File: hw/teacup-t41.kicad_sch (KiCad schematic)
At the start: 104 parts, among them IC1 T31ZX, J1 USB Type-C, J10 AudioJack4_Ground, J11 Conn_01x04_Pin, J12 Conn_01x04_Pin, J13 SFW15R-2STE1LF, J14 Conn_01x02_MountingPin, J15 Conn_01x03_MountingPin, J16 Conn_01x03_MountingPin, J2 Micro_SD_Card, J3 USB_A, J4 Conn_02x08_Odd_Even, J5 UART, J6 Conn_02x07_Odd_Even, J7 Conn_02x07_Odd_Even, J8 DC_IN, J9 Conn_01x02_MountingPin, SW2 SW_SPDT, U1 AZ1117-3.3, U2 AZ1117-1.8, U3 MCP1826S, U4 W25Q32JVSS, U5 W25Q32JVSS, Y1 24 MHz

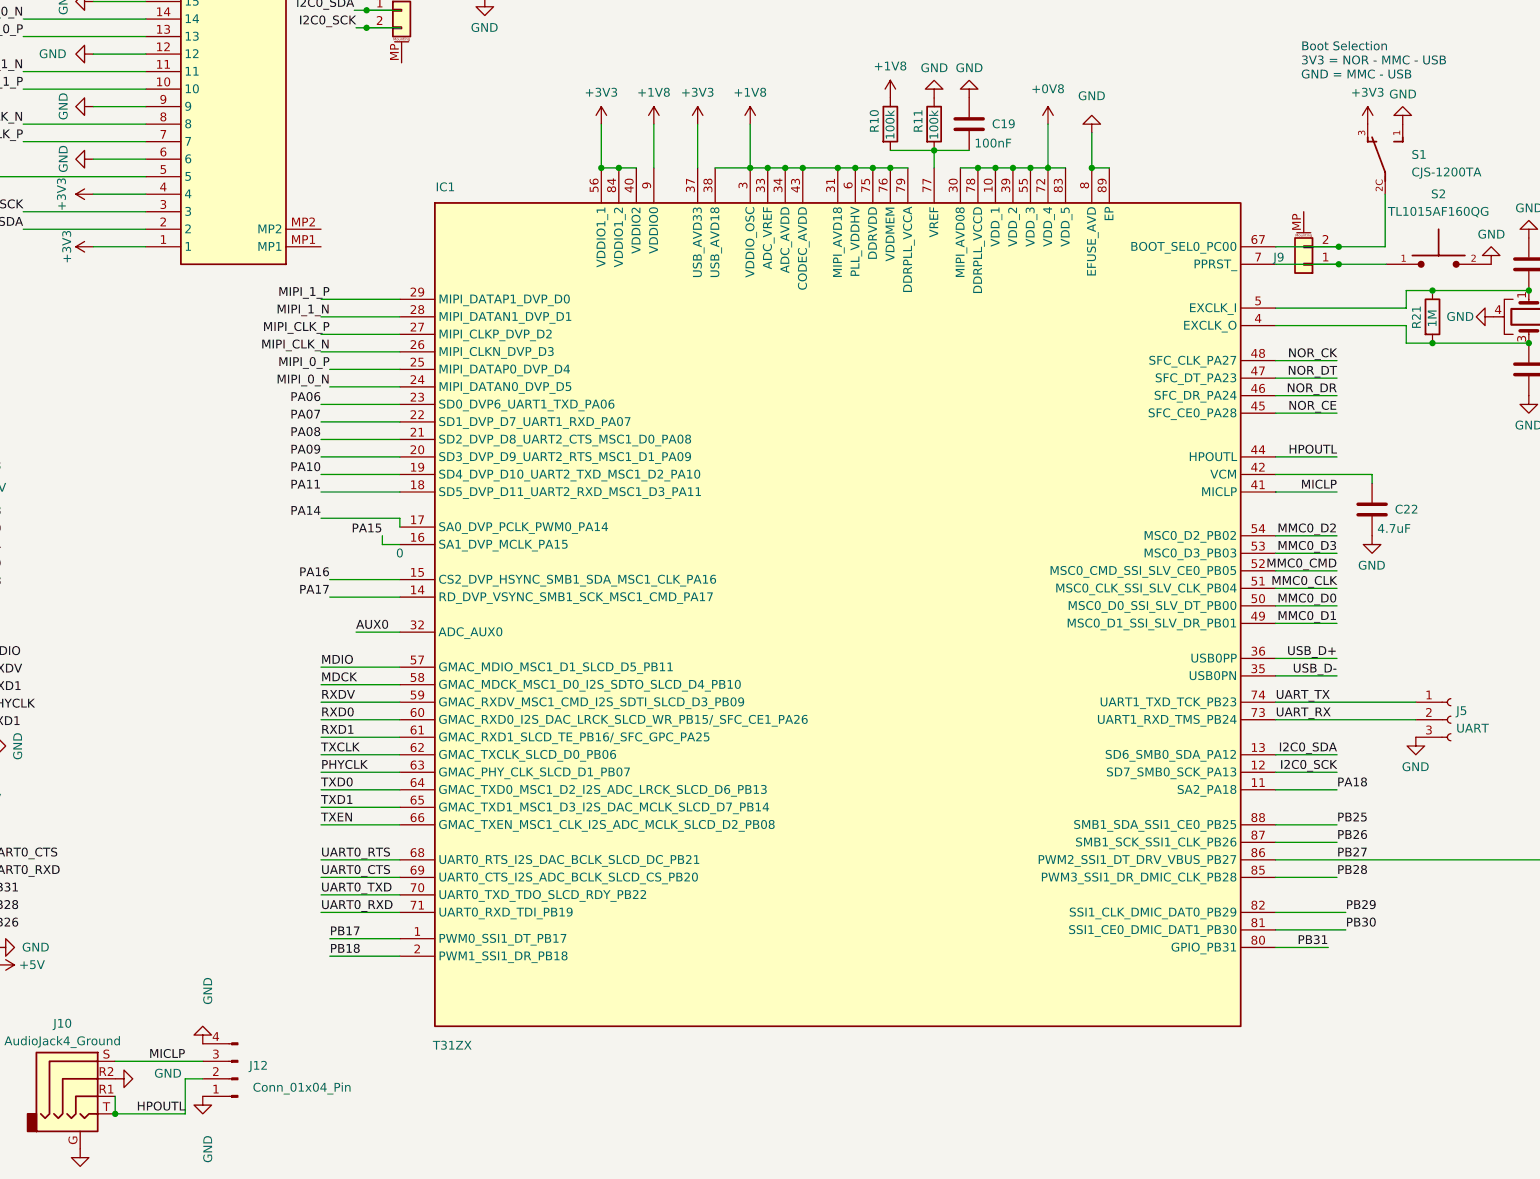
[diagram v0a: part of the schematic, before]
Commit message: Swap IC1 T31ZX->T41NQ in schematic, rewire by net-name
Label-driven rewire: T41NQ symbol placed, every pin connected per
t41_pin_nets.csv. 6 wire-only nets (crystal, boot-sel, VCM, DDR-VREF
divider, PB27/SD) re-anchored with reconnection labels; other stubs
removed with their inert far-labels. Auto-named nets given clean labels
(EXCLK_XIN/XOUT, BOOT_SEL0, VCM, DDR_VREF).

Verified via netlist export: all 97 IC1 pins on intended nets (0
mismatch), 0 peripheral nodes lost vs upstream (PPRST intentionally
dropped). Remaining ERC errors are pre-power-section: floating new
nets (DDR_ZQ/RZQ/POR_CTL/MICNL/NOR_WP/HOLD) + undriven +1V35 await
the power/new-circuit stage. gen_schematic.py in scripts/.
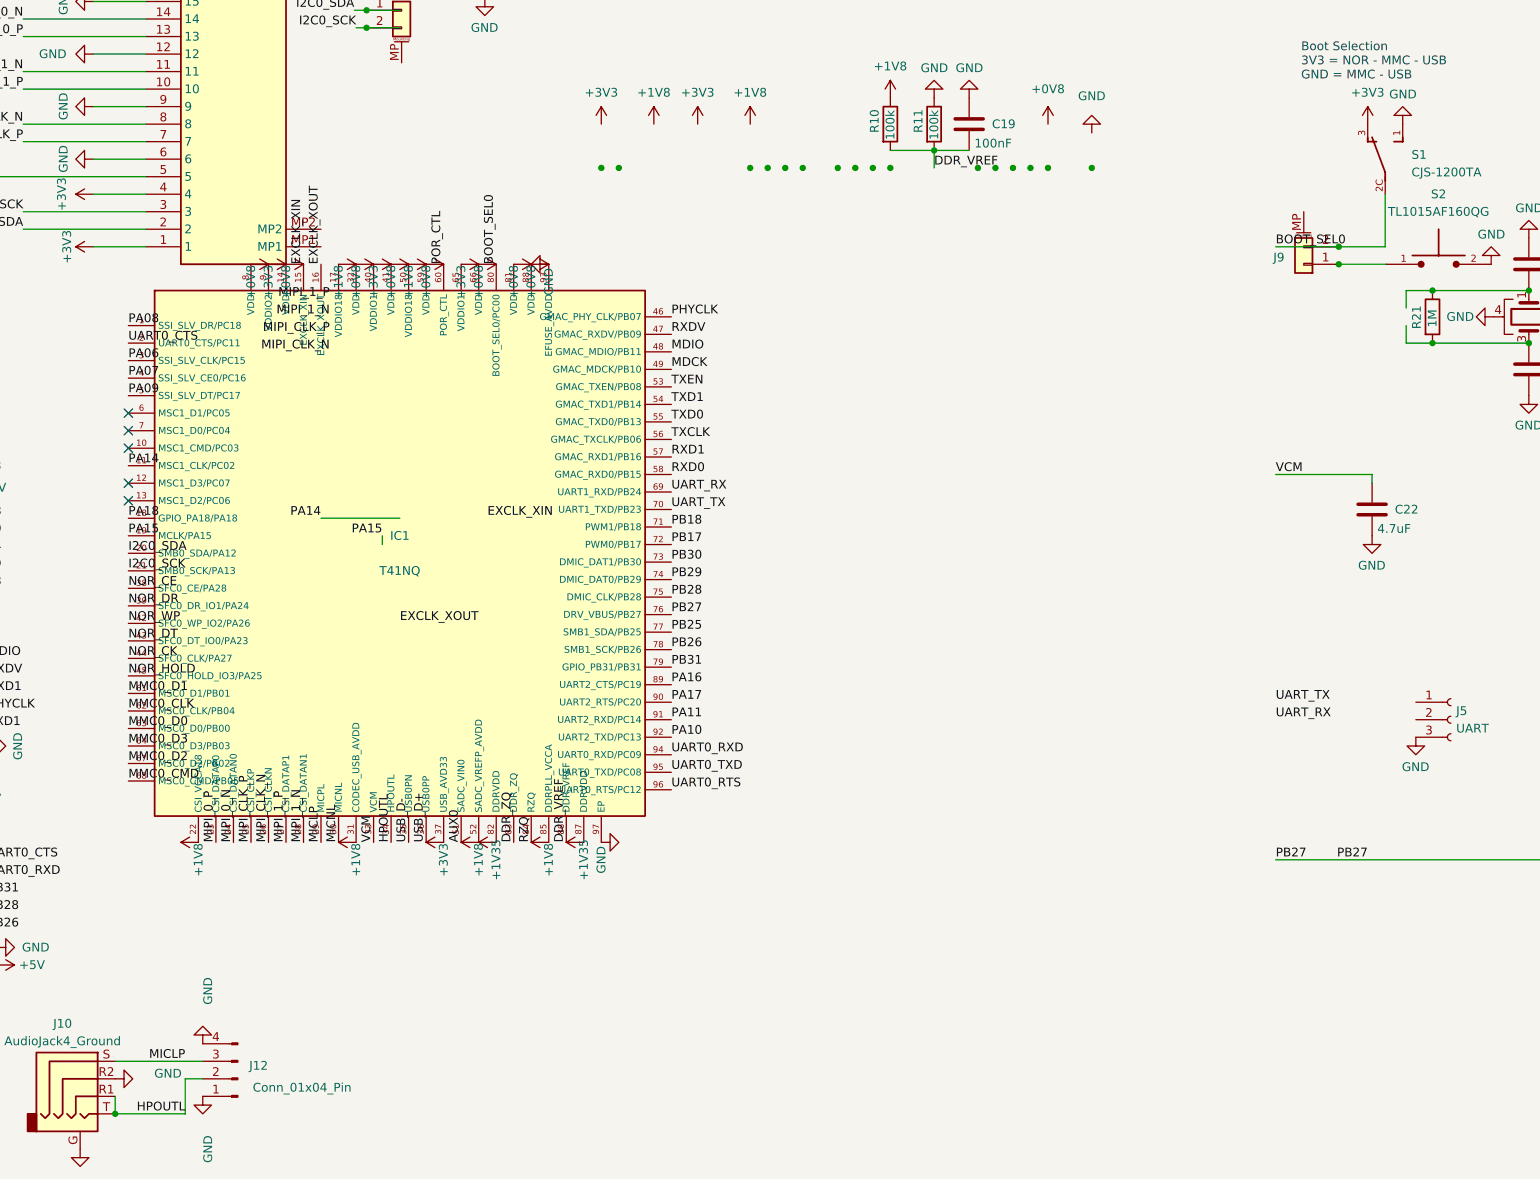
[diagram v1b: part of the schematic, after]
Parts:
- removed IC1: T31ZX, teacup:QFN35P900X900X90-89N-D, symbol teacup:T31ZX
- added IC1: T41NQ, teacup:QFN96_10x10_P0.35_EP7.6x7.2_T41, symbol teacup:T41NQ
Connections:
- net +0V8: now also IC1.14 (VDD), IC1.32 (VDD), IC1.41 (VDD), IC1.59 (VDD), IC1.66 (VDD), IC1.8 (VDD), IC1.81 (VDD), IC1.88 (VDD)
- net +1V8: now also IC1.17 (VDDIO18), IC1.22 (CSI_VCCA18), IC1.31 (CODEC_USB_AVDD), IC1.50 (VDDIO18), IC1.52 (SADC_VREFP_AVDD), IC1.85 (DDRPLL_VCCA)
- net +3V3: now also IC1.37 (USB_AVD33), IC1.40 (VDDIO1), IC1.65 (VDDIO1), IC1.9 (VDDIO2)
- net AUX0: now also IC1.51 (SADC_VIN0)
- net GND: now also IC1.93 (EFUSE_AVDD), IC1.97 (EP)
- net HPOUTL: now also IC1.34 (HPOUTL)
- net I2C0_SCK: now also IC1.21 (SMB0_SCK/PA13)
- net I2C0_SDA: now also IC1.20 (SMB0_SDA/PA12)
- net MDCK: now also IC1.49 (GMAC_MDCK/PB10)
- net MDIO: now also IC1.48 (GMAC_MDIO/PB11)
- net MICLP: now also IC1.29 (MICPL)
- net MIPI_0_N: now also IC1.24 (CSI_DATAN0)
- net MIPI_0_P: now also IC1.23 (CSI_DATAP0)
- net MIPI_1_N: now also IC1.28 (CSI_DATAN1)
- net MIPI_1_P: now also IC1.27 (CSI_DATAP1)
- net MIPI_CLK_N: now also IC1.26 (CSI_CLKN)
- net MIPI_CLK_P: now also IC1.25 (CSI_CLKP)
- net MMC0_CLK: now also IC1.62 (MSC0_CLK/PB04)
- net MMC0_CMD: now also IC1.68 (MSC0_CMD/PB05)
- net MMC0_D0: now also IC1.63 (MSC0_D0/PB00)
- net MMC0_D1: now also IC1.61 (MSC0_D1/PB01)
- net MMC0_D2: now also IC1.67 (MSC0_D2/PB02)
- net MMC0_D3: now also IC1.64 (MSC0_D3/PB03)
- net NOR_CE: now also IC1.38 (SFC0_CE/PA28)
- net NOR_CK: now also IC1.44 (SFC0_CLK/PA27)
- net NOR_DR: now also IC1.39 (SFC0_DR_IO1/PA24)
- net NOR_DT: now also IC1.43 (SFC0_DT_IO0/PA23)
- net PA06: now also IC1.3 (SSI_SLV_CLK/PC15)
- net PA07: now also IC1.4 (SSI_SLV_CE0/PC16)
- net PA08: now also IC1.1 (SSI_SLV_DR/PC18)
- net PA09: now also IC1.5 (SSI_SLV_DT/PC17)
- net PA10: now also IC1.92 (UART2_TXD/PC13)
- net PA11: now also IC1.91 (UART2_RXD/PC14)
- net PA14: now also IC1.11 (MSC1_CLK/PC02)
- net PA15: now also IC1.19 (MCLK/PA15)
- net PA16: now also IC1.89 (UART2_CTS/PC19)
- net PA17: now also IC1.90 (UART2_RTS/PC20)
- net PA18: now also IC1.18 (GPIO_PA18/PA18)
- net PB17: now also IC1.72 (PWM0/PB17)
- net PB18: now also IC1.71 (PWM1/PB18)
- net PB25: now also IC1.77 (SMB1_SDA/PB25)
- net PB26: now also IC1.78 (SMB1_SCK/PB26)
- net PB27: now also IC1.76 (DRV_VBUS/PB27)
- net PB28: now also IC1.75 (DMIC_CLK/PB28)
- net PB29: now also IC1.74 (DMIC_DAT0/PB29)
- net PB30: now also IC1.73 (DMIC_DAT1/PB30)
- net PB31: now also IC1.79 (GPIO_PB31/PB31)
- net PHYCLK: now also IC1.46 (GMAC_PHY_CLK/PB07)
- net RXD0: now also IC1.58 (GMAC_RXD0/PB15)
- net RXD1: now also IC1.57 (GMAC_RXD1/PB16)
- net RXDV: now also IC1.47 (GMAC_RXDV/PB09)
- net TXCLK: now also IC1.56 (GMAC_TXCLK/PB06)
- net TXD0: now also IC1.55 (GMAC_TXD0/PB13)
- net TXD1: now also IC1.54 (GMAC_TXD1/PB14)
- net TXEN: now also IC1.53 (GMAC_TXEN/PB08)
- net UART0_CTS: now also IC1.2 (UART0_CTS/PC11)
- net UART0_RTS: now also IC1.96 (UART0_RTS/PC12)
- net UART0_RXD: now also IC1.94 (UART0_RXD/PC09)
- net UART0_TXD: now also IC1.95 (UART0_TXD/PC08)
- net UART_RX: now also IC1.69 (UART1_RXD/PB24); no longer J5.2 (Pin_2)
- net UART_TX: now also IC1.70 (UART1_TXD/PB23); no longer J5.1 (Pin_1)
- net USB_D+: now also IC1.36 (USB0PP)
- net USB_D-: now also IC1.35 (USB0PN)
- net DDR_VREF: now reaches C19.2, R10.2, R11.2
- net DDR_VREF: now also IC1.86 (DDR_VREF)
- net BOOT_SEL0: now reaches J9.2 (Pin_2), S1.2C
- net BOOT_SEL0: now also IC1.80 (BOOT_SEL0/PC00)
- net VCM: now reaches C22.1
- net VCM: now also IC1.33 (VCM)
- new net +1V35: IC1.82 (DDRVDD), IC1.87 (DDRVDD)
- new net DDR_ZQ: IC1.83 (DDR_ZQ)
- new net EXCLK_XIN: IC1.15 (EXCLK_XIN)
- new net EXCLK_XOUT: IC1.16 (EXCLK_XOUT)
- new net MICNL: IC1.30 (MICNL)
- new net NOR_HOLD: IC1.45 (SFC0_HOLD_IO3/PA25)
- new net NOR_WP: IC1.42 (SFC0_WP_IO2/PA26)
- new net POR_CTL: IC1.60 (POR_CTL)
- new net RZQ: IC1.84 (RZQ)
- no-connect marks 1 -> 6
